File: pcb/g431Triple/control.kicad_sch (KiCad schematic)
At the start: 30 parts, among them J1 USB_C_Receptacle_USB2.0, P1 FTSH-107-01-L-DV-K, P2 ST-Link, P3 AFC07-S24FCC-00, SW1 RotaryEncoder_Switch, U1 STM32G431CBUx, U2 TPS82130, U3 BME680, U7 TSOP38338, U8 TSOP38338

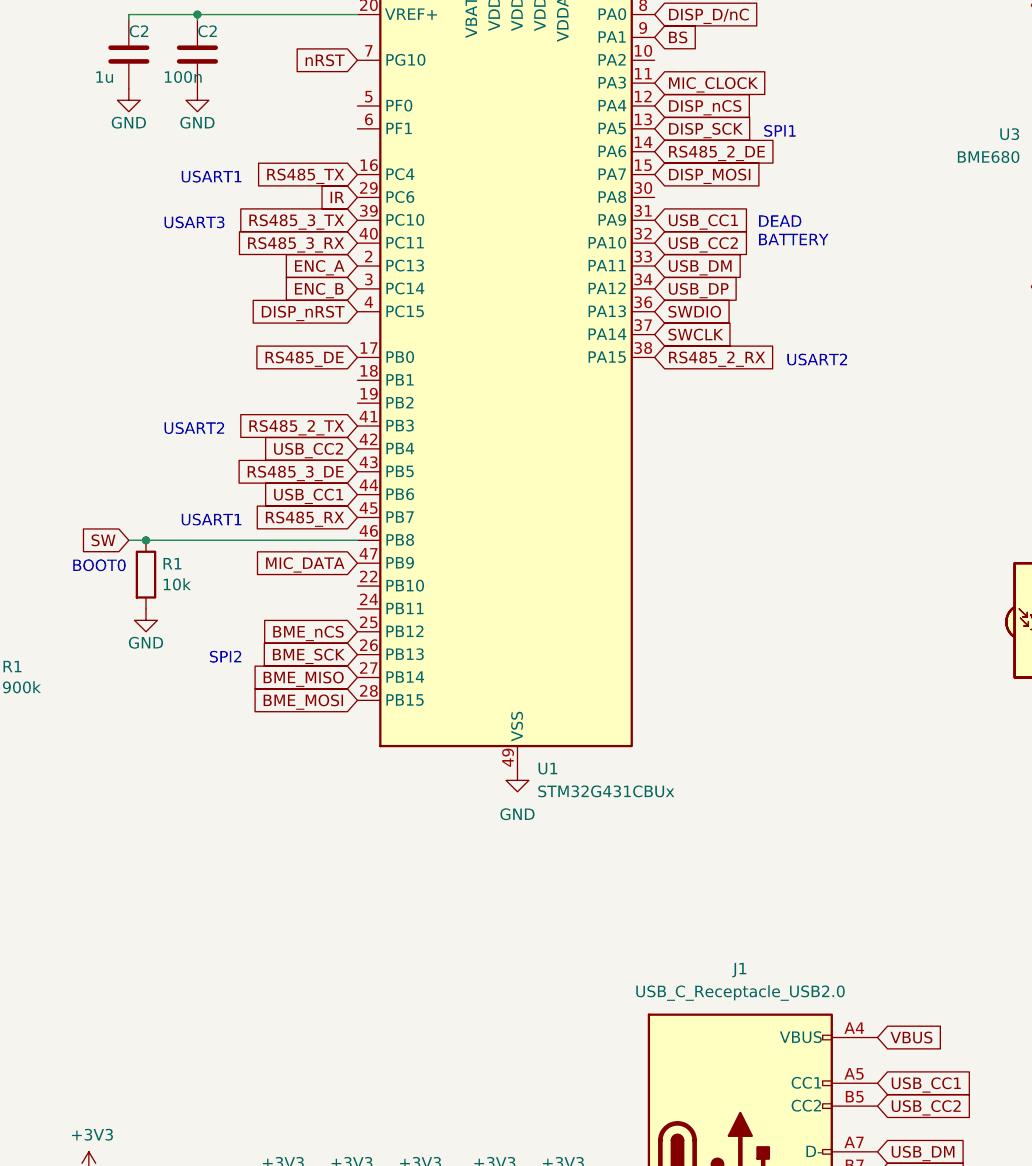
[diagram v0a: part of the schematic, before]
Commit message: Rename to g431/g431Triple, new pin ordering for Harting connector
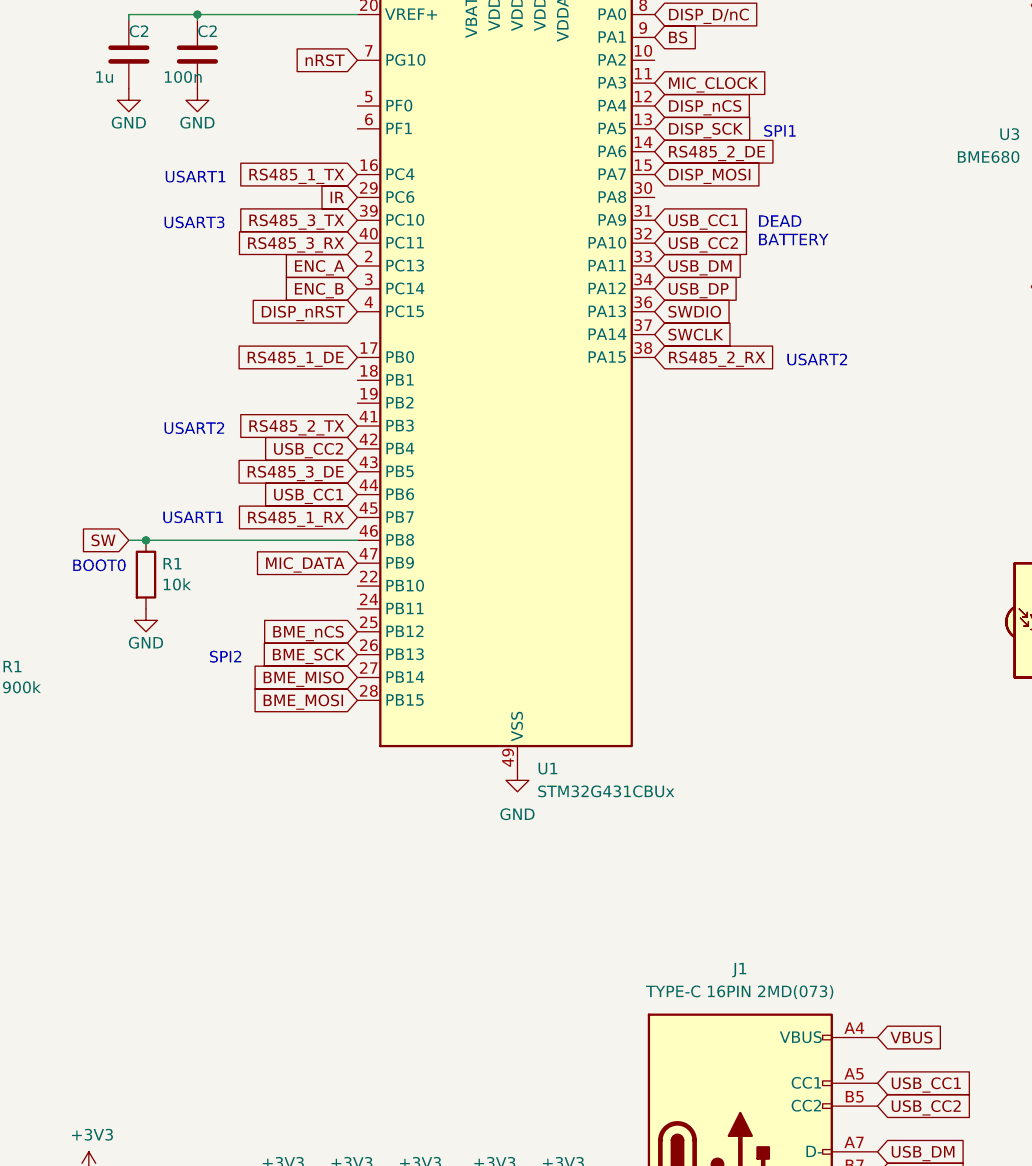
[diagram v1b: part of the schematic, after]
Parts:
- J1: value USB_C_Receptacle_USB2.0 -> TYPE-C 16PIN 2MD(073); now in the parts list
- U7, U8: now left out of the parts list
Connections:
- net RS485_DE renamed RS485_1_DE
- net RS485_RX renamed RS485_1_RX
- net RS485_TX renamed RS485_1_TX
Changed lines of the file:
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@@
 	)
 	(junction
+		(at 185.42 100.33)
+		(diameter 0)
+		(color 0 0 0 0)
+	)
+	(junction
 		(at 251.46 94.615)
 		(diameter 0)
@@
 	)
 	(junction
-		(at 185.42 110.49)
-		(diameter 0)
-		(color 0 0 0 0)
-	)
-	(junction
 		(at 26.67 167.005)
 		(diameter 0)
@@
 	)
 	(junction
-		(at 185.42 100.33)
-		(diameter 0)
-		(color 0 0 0 0)
-	)
-	(junction
 		(at 54.61 182.245)
 		(diameter 0)
@@
 	)
 	(junction
+		(at 185.42 110.49)
+		(diameter 0)
+		(color 0 0 0 0)
+	)
+	(junction
 		(at 33.02 116.84)
 		(diameter 0)
@@
 	(text "USART1"
 		(exclude_from_sim no)
-		(at 72.39 95.25 0)
+		(at 70.358 94.996 0)
 		(effects
 			(font
@@
 	(text "USART1"
 		(exclude_from_sim no)
-		(at 72.39 57.15 0)
+		(at 70.612 57.15 0)
 		(effects
 			(font
@@
 		)
 	)
-	(global_label "RS485_RX"
+	(global_label "RS485_1_RX"
 		(shape input)
 		(at 92.075 93.98 180)
@@
 		)
 	)
-	(global_label "RS485_DE"
+	(global_label "RS485_1_DE"
 		(shape input)
 		(at 92.075 76.2 180)
@@
 		)
 	)
-	(global_label "RS485_TX"
+	(global_label "RS485_1_TX"
 		(shape input)
 		(at 92.075 55.88 180)
@@
 		(unit 1)
 		(exclude_from_sim no)
-		(in_bom yes)
+		(in_bom no)
 		(on_board yes)
 		(dnp no)
@@
 		(unit 1)
 		(exclude_from_sim no)
-		(in_bom yes)
+		(in_bom no)
 		(on_board yes)
 		(dnp no)
@@
 		(unit 1)
 		(exclude_from_sim no)
-		(in_bom no)
+		(in_bom yes)
 		(on_board yes)
 		(dnp no)
@@
 			)
 		)
-		(property "Value" "USB_C_Receptacle_USB2.0"
+		(property "Value" "TYPE-C 16PIN 2MD(073)"
 			(at 134.62 146.685 0)
 			(effects

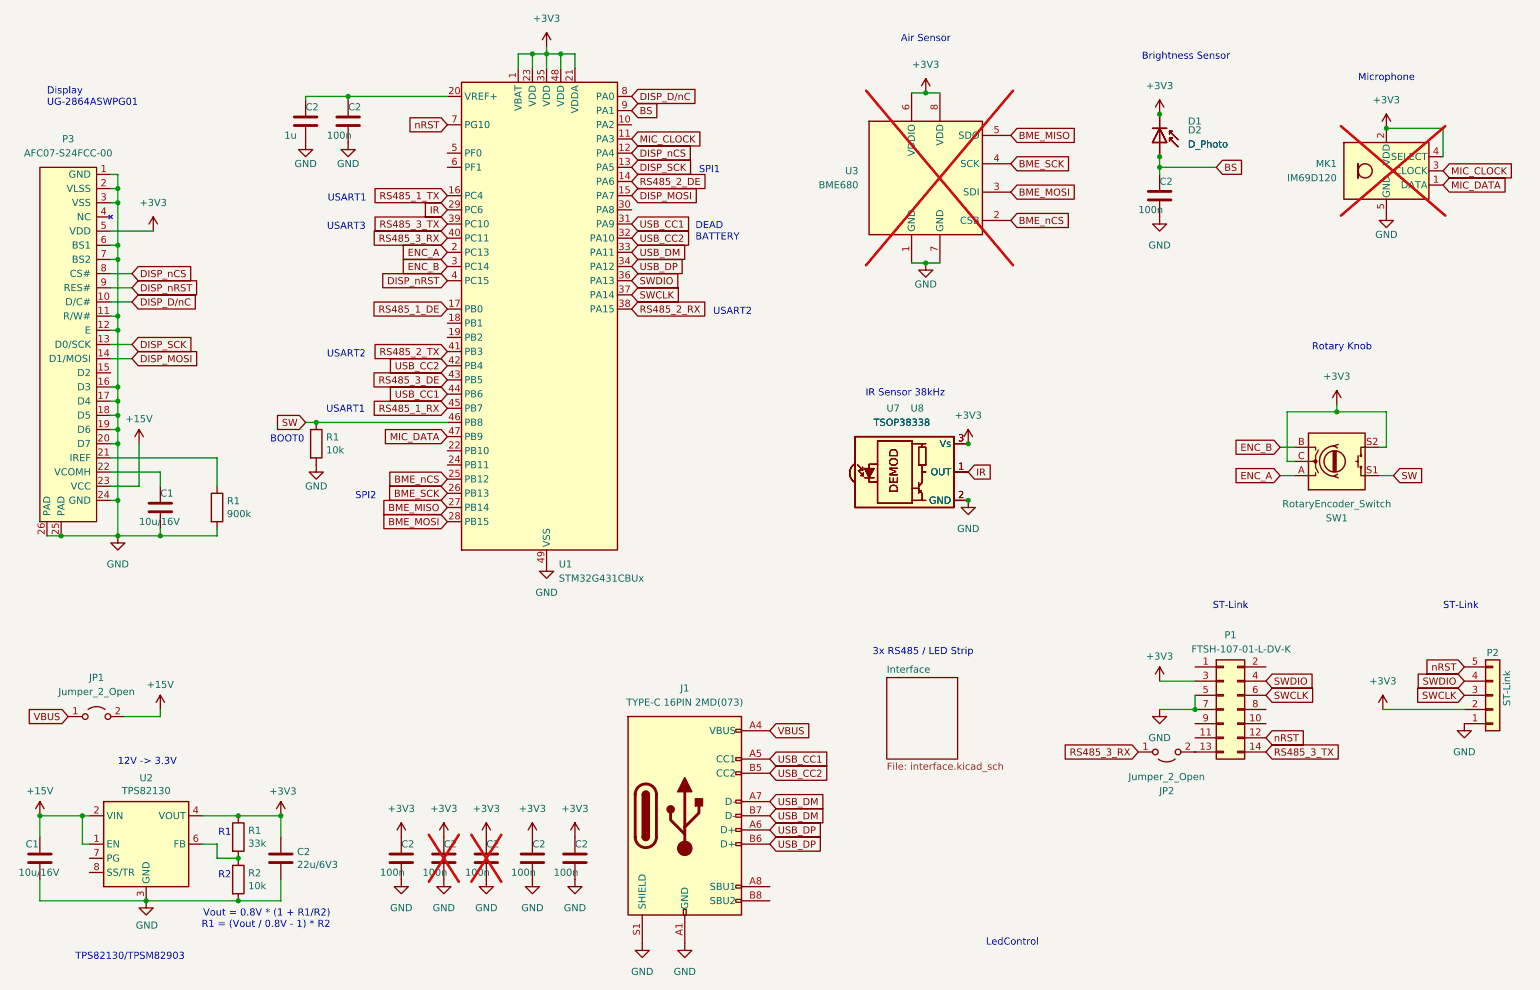
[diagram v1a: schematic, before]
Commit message: Multiple led strips
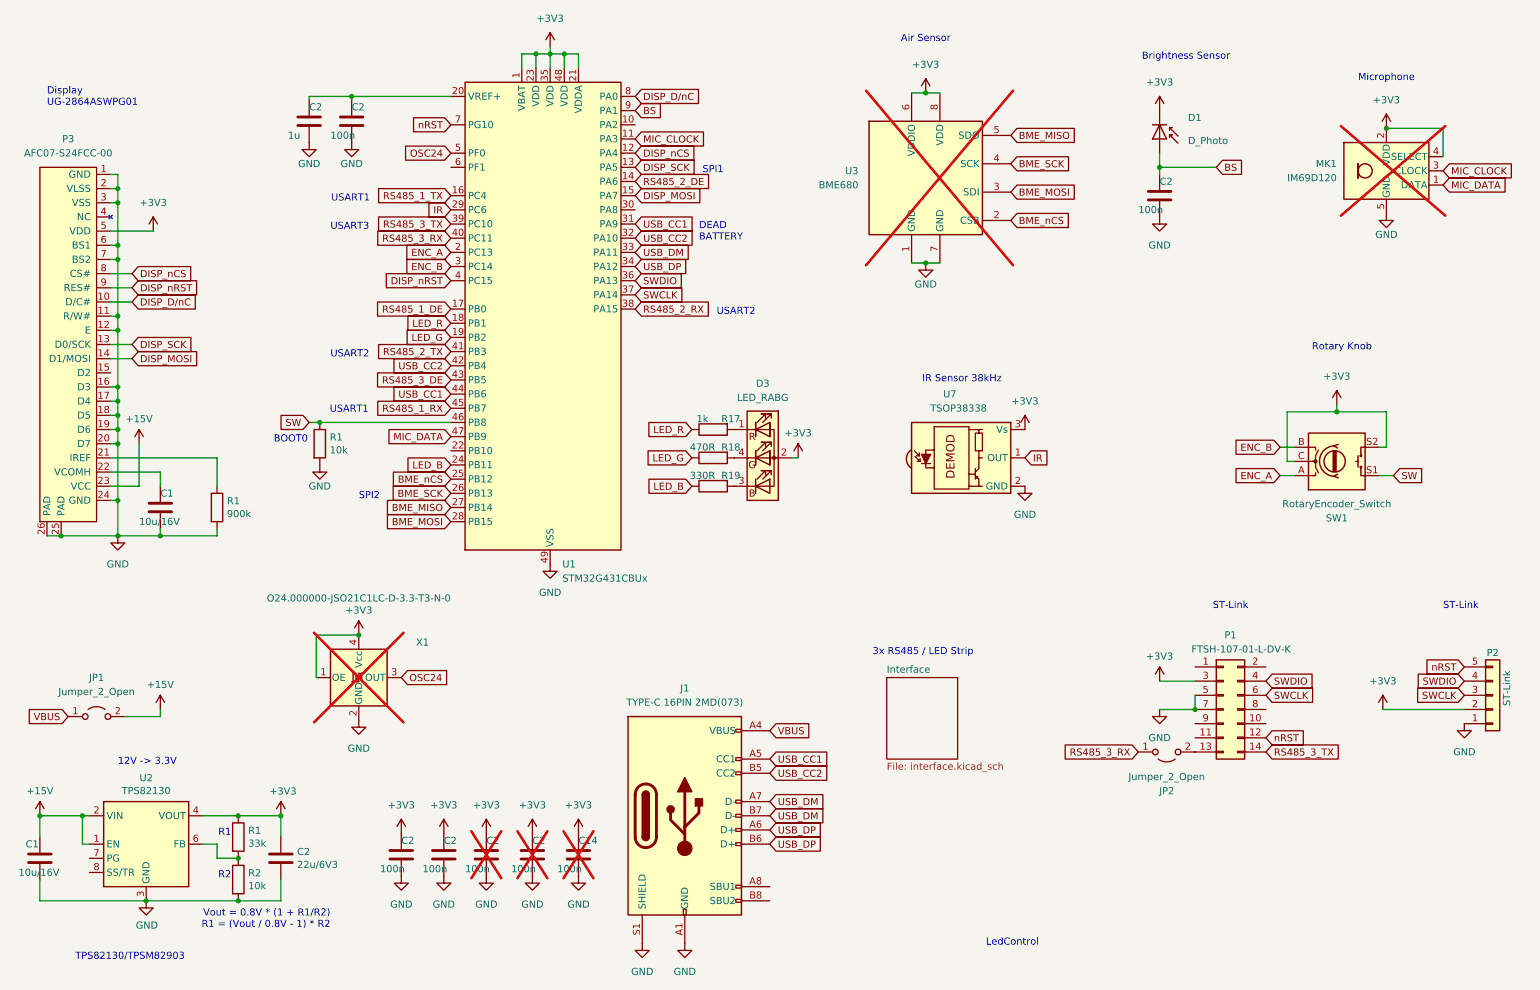
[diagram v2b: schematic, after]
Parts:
- removed C2: 100n, local:0603, symbol Device:C
- removed D2: D_Photo, local:PhotoDiode, symbol Device:D_Photo
- removed U8: TSOP38338, local:TSOP38338, symbol Interface_Optical:TSOP382xx
- added C14: 100n, local:0603, symbol Device:C
- added D3: LED_RABG, LED_THT:LED_D5.0mm-4_RGB, symbol Device:LED_RABG
- added R17: 1k, local:0603, symbol Device:R
- added R18: 470R, local:0603, symbol Device:R
- added R19: 330R, local:0603, symbol Device:R
- added X1: O24.000000-JSO21C1LC-D-3.3-T3-N-0, local:JSO21, symbol Oscillator:SG-8002JA
- C2: now fitted
- C2: now not fitted
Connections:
- net +3V3: now also C14.1, D3.2 (A), X1.1 (OE), X1.4 (Vcc)
- net GND: now also C14.2, X1.2 (GND)
- net LED_R: now reaches U1.18 (PB1)
- net LED_R: now also R17.1
- net LED_G: now reaches U1.19 (PB2)
- net LED_G: now also R18.1
- net LED_B: now reaches U1.24 (PB11)
- net LED_B: now also R19.1
- net OSC24: now reaches U1.5 (PF0)
- net OSC24: now also X1.3 (OUT)
- new net: D3.4 (GK), R18.2
- new net: D3.1 (RK), R17.2
- new net: D3.3 (BK), R19.2
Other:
- moved on the sheet: C2, D1, R1, U1, U7

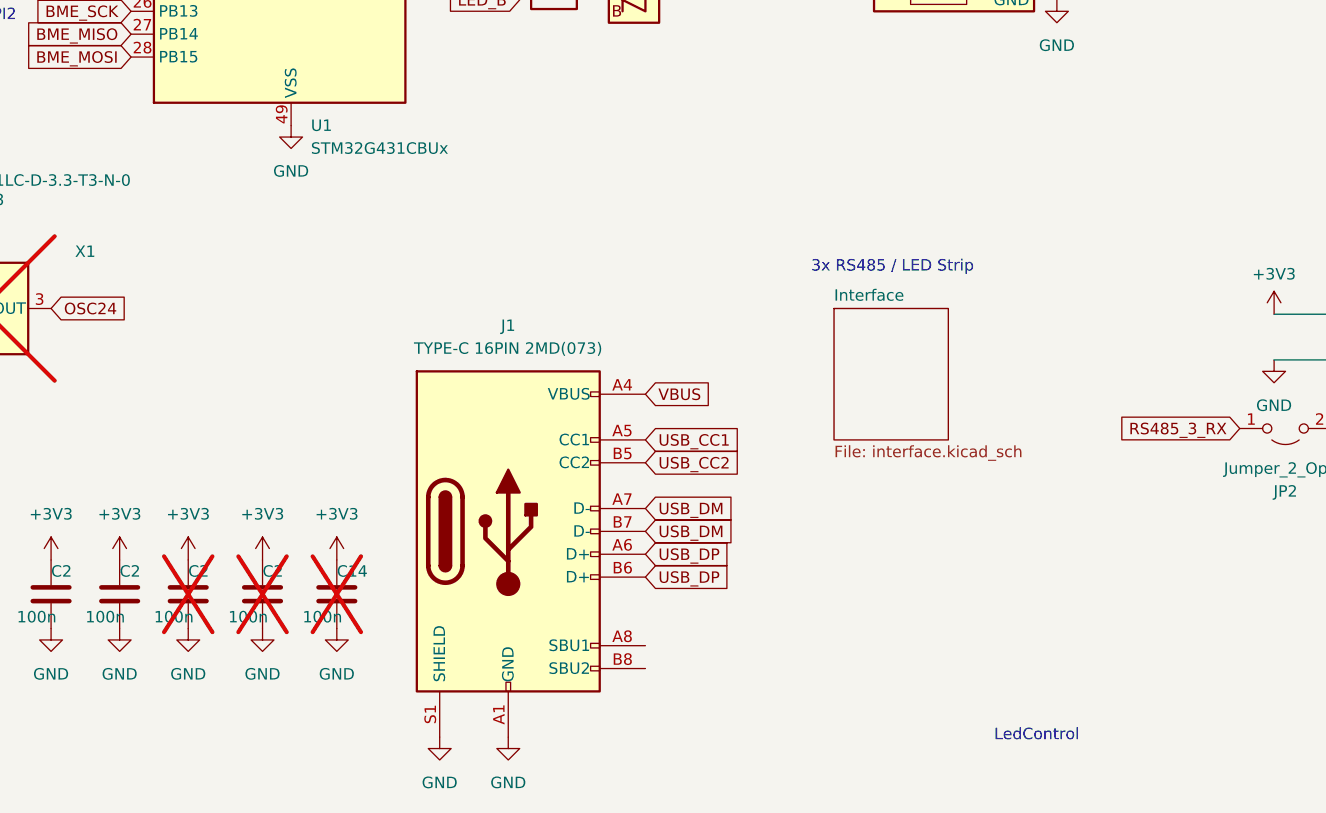
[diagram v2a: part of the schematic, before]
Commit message: Add color temperature
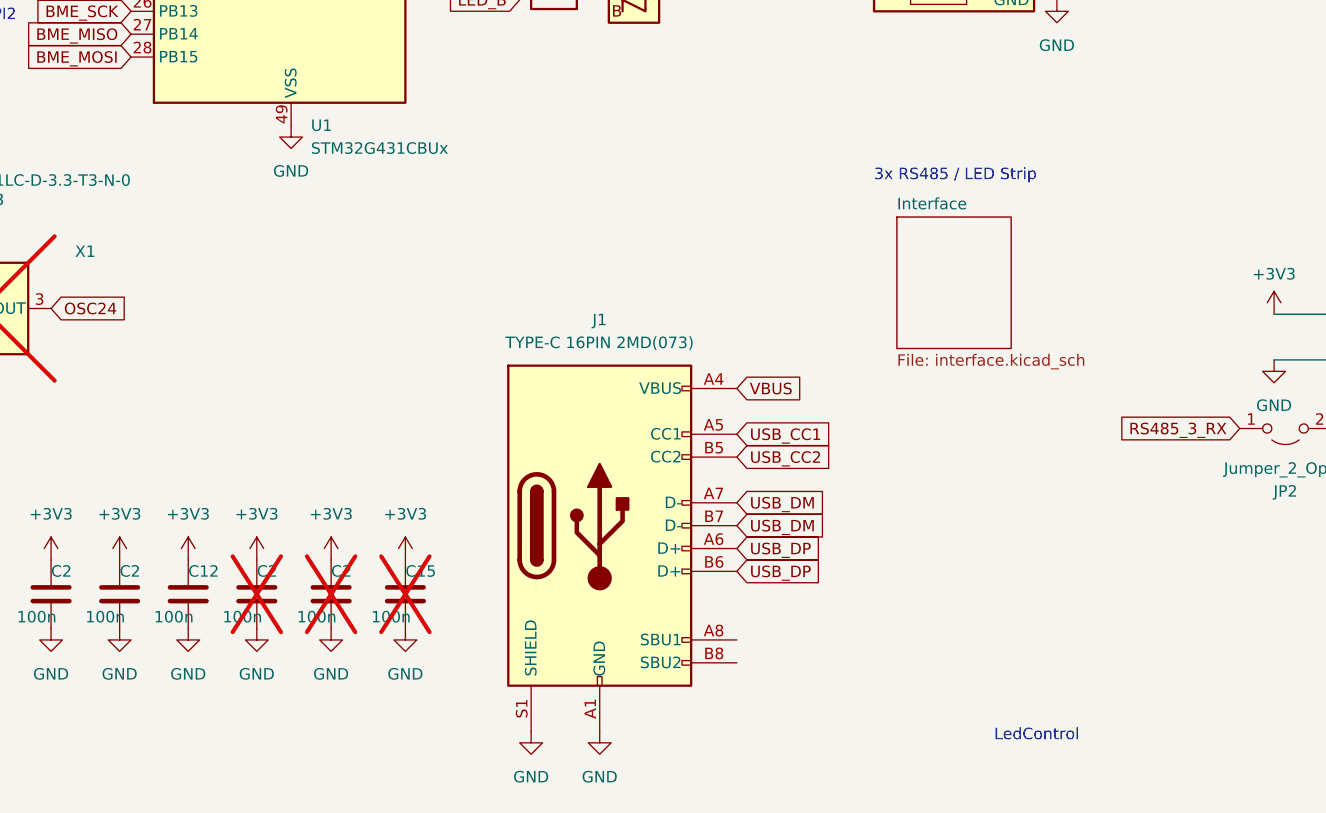
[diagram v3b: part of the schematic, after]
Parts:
- added C12: 100n, local:0603, symbol Device:C
- renumbered C14 to C15
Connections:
- net +3V3: now also C12.1
- net GND: now also C12.2
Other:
- moved on the sheet: C15, C2, J1

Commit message: Start preset name editor
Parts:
- C12, C15, C2: symbol Device:C -> Device:C_Small
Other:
- moved on the sheet: C15, C2
